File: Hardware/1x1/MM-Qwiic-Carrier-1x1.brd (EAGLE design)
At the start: 80 x 35.6 mm, 87 parts, among them J15 MICROMOD-2222-C, J2 QWIIC_RIGHT_ANGLE, J5 Vertical Qwiic Connector, U1 MCP73831, U5 AP7361C-33FGEUDFN-8

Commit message: Run of engineering checklist
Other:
- board text added: "v10"
- board text removed: "v01"
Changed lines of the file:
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@@
 <board>
 <plain>
-<wire x1="0" y1="0" x2="0" y2="35.56" width="0.254" layer="20"/>
-<wire x1="0" y1="35.56" x2="80.01" y2="35.56" width="0.254" layer="20"/>
-<wire x1="80.01" y1="35.56" x2="80.01" y2="0" width="0.254" layer="20"/>
-<wire x1="80.01" y1="0" x2="0" y2="0" width="0.254" layer="20"/>
-<text x="7.62" y="1.016" size="1.27" layer="16" font="vector" ratio="20" rot="MR180" align="center">v01</text>
+<wire x1="0" y1="0" x2="0" y2="35.56" width="0.2032" layer="20"/>
+<wire x1="0" y1="35.56" x2="80.01" y2="35.56" width="0.2032" layer="20"/>
+<wire x1="80.01" y1="35.56" x2="80.01" y2="0" width="0.2032" layer="20"/>
+<wire x1="80.01" y1="0" x2="0" y2="0" width="0.2032" layer="20"/>
+<text x="7.62" y="1.016" size="1.27" layer="16" font="vector" ratio="20" rot="MR180" align="center">v10</text>
 <wire x1="27.94" y1="28.829" x2="44.185" y2="28.829" width="0.2032" layer="21"/>
 <wire x1="44.185" y1="28.829" x2="44.185" y2="6.731" width="0.2032" layer="21"/>

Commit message: Changes from design review
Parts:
- J6: device SparkFun-Connectors:1X08_NO_SILK -> SparkFun-Connectors:1X09_NO_SILK
- moved J6 2.54 mm to (22.9, 34.3)
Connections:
- net 3.3V: now also J6.1
- net D0: now also J6.4; no longer J6.3
- net D1: now also J6.5; no longer J6.4
- net GND: now also J6.2; no longer J6.1
- net I2C_!INT!: now also J6.3; no longer J6.2
- net SPI_!CS!: now also J6.9; no longer J6.8
- net SPI_CIPO: now also J6.6; no longer J6.5
- net SPI_COPI: now also J6.7; no longer J6.6
- net SPI_SCK: now also J6.8; no longer J6.7
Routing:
- net 3.3V: track 78.8 -> 82.8 mm
- net VIN: track 30.6 -> 29.3 mm
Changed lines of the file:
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@@
 <layer number="29" name="tStop" color="7" fill="3" visible="no" active="yes"/>
 <layer number="30" name="bStop" color="7" fill="6" visible="no" active="yes"/>
-<layer number="31" name="tCream" color="7" fill="4" visible="yes" active="yes"/>
+<layer number="31" name="tCream" color="7" fill="4" visible="no" active="yes"/>
 <layer number="32" name="bCream" color="7" fill="5" visible="no" active="yes"/>
 <layer number="33" name="tFinish" color="6" fill="3" visible="no" active="yes"/>
@@
 <attribute name="VALUE" x="46.212" y="5.86833125" size="0.6096" layer="27" rot="R180"/>
 </element>
-<element name="J6" library="SparkFun-Connectors" package="1X08_NO_SILK" value="" x="25.4" y="34.29" smashed="yes">
-<attribute name="NAME" x="24.13" y="35.687" size="0.6096" layer="25" font="vector" ratio="20"/>
-<attribute name="PROD_ID" value="CONN-08438" x="25.4" y="34.29" size="1.778" layer="27" font="vector" ratio="15" display="off"/>
-<attribute name="VALUE" x="24.13" y="32.258" size="0.6096" layer="27" font="vector" ratio="20"/>
-</element>
 <element name="U$5" library="SparkFun-Boards" package="QWIIC_BOARD_MOUNT_SMD_STANDOFFS" value="QWIIC_BOARD_OUTLINESTANDOFF" x="62.23" y="17.78" smashed="yes"/>
 <element name="U$10" library="output" package="QWIIC_CARRIER_#_1X10" value="" x="51.308" y="2.413" smashed="yes"/>
@@
 <element name="U$20" library="output" package="#D1#0" value="" x="33.02" y="30.734" smashed="yes" rot="R90"/>
 <element name="U$21" library="output" package="#D1#0" value="" x="33.02" y="30.734" smashed="yes" rot="MR90"/>
+<element name="J6" library="SparkFun-Connectors" package="1X09_NO_SILK" value="" x="22.86" y="34.29" smashed="yes">
+<attribute name="NAME" x="21.59" y="35.687" size="0.6096" layer="25" font="vector" ratio="20"/>
+<attribute name="VALUE" x="21.59" y="32.258" size="0.6096" layer="27" font="vector" ratio="20"/>
+</element>
 </elements>
 <signals>
@@
 <contactref element="J4" pad="2"/>
 <contactref element="J5" pad="1"/>
-<contactref element="J6" pad="1"/>
 <via x="17.526" y="27.94" extent="1-16" drill="0.3048"/>
 <via x="3.81" y="24.13" extent="1-16" drill="0.3048"/>
@@
 <via x="20.447" y="16.637" extent="1-16" drill="0.3048"/>
 <via x="24.638" y="17.272" extent="1-16" drill="0.3048"/>
+<contactref element="J6" pad="2"/>
 </signal>
 <signal name="3.3V">
@@
 <wire x1="24.6507" y1="26.0477" x2="23.5077" y2="26.0477" width="0.4064" layer="1"/>
 <wire x1="23.5077" y1="26.0477" x2="23.5077" y2="10.738625" width="0.4064" layer="1"/>
-<wire x1="15.875" y1="31.242" x2="20.32" y2="31.242" width="0.4064" layer="16"/>
 <via x="23.5077" y="26.0477" extent="1-16" drill="0.3048"/>
-<wire x1="23.5077" y1="26.0477" x2="22.6681125" y2="26.0477" width="0.4064" layer="16"/>
-<wire x1="22.6681125" y1="26.0477" x2="22.314" y2="26.4018125" width="0.4064" layer="16"/>
-<wire x1="20.32" y1="31.242" x2="22.314" y2="29.248" width="0.4064" layer="16"/>
-<wire x1="22.314" y1="29.248" x2="22.314" y2="26.4018125" width="0.4064" layer="16"/>
 <wire x1="37.6" y1="5.08" x2="37.6" y2="3.437" width="0.4064" layer="1"/>
 <wire x1="37.6" y1="3.437" x2="37.592" y2="3.429" width="0.4064" layer="1"/>
@@
 <wire x1="26.405" y1="8.78" x2="27.542" y2="8.78" width="0.2032" layer="1"/>
 <wire x1="27.542" y1="8.78" x2="35.162" y2="8.78" width="0.4064" layer="1"/>
+<contactref element="J6" pad="1"/>
+<wire x1="22.86" y1="34.29" x2="22.86" y2="31.242" width="0.4064" layer="16"/>
+<wire x1="22.86" y1="31.242" x2="22.86" y2="26.6954" width="0.4064" layer="16"/>
+<wire x1="22.86" y1="26.6954" x2="23.5077" y2="26.0477" width="0.4064" layer="16"/>
+<wire x1="15.875" y1="31.242" x2="22.86" y2="31.242" width="0.4064" layer="16"/>
 </signal>
 <signal name="USB_D-">
@@
 <wire x1="13.97" y1="11.85" x2="13.97" y2="10.668" width="0.4064" layer="1"/>
 <via x="13.97" y="10.668" extent="1-16" drill="0.3048"/>
-<wire x1="13.97" y1="10.668" x2="12.192" y2="10.668" width="0.4064" layer="16"/>
-<wire x1="10.668" y1="12.192" x2="9.906" y2="12.192" width="0.4064" layer="16"/>
-<wire x1="9.906" y1="12.192" x2="9.525" y2="12.573" width="0.4064" layer="16"/>
-<wire x1="9.525" y1="12.573" x2="9.525" y2="14.224" width="0.4064" layer="16"/>
-<wire x1="9.7885" y1="14.4875" x2="10.2965" y2="14.4875" width="0.4064" layer="16"/>
-<wire x1="9.7885" y1="14.4875" x2="9.525" y2="14.224" width="0.4064" layer="16"/>
 <via x="10.2965" y="14.4875" extent="1-16" drill="0.3048"/>
-<wire x1="12.192" y1="10.668" x2="10.668" y2="12.192" width="0.4064" layer="16"/>
 <wire x1="13.97" y1="10.668" x2="13.97" y2="10.65786875" width="0.2032" layer="1"/>
 <wire x1="14.09786875" y1="10.53" x2="13.97" y2="10.65786875" width="0.2032" layer="1"/>
@@
 <wire x1="10.03" y1="21.968" x2="10.03" y2="19.05" width="0.4064" layer="1"/>
 <wire x1="11.43" y1="23.368" x2="10.03" y2="21.968" width="0.4064" layer="1"/>
+<wire x1="10.2965" y1="14.4875" x2="12.1825" y2="14.4875" width="0.4064" layer="16"/>
+<wire x1="12.1825" y1="14.4875" x2="13.97" y2="12.7" width="0.4064" layer="16"/>
+<wire x1="13.97" y1="12.7" x2="13.97" y2="10.668" width="0.4064" layer="16"/>
 </signal>
 <signal name="N$1">
@@
 </signal>
 <signal name="I2C_!INT!">
-<contactref element="J6" pad="2"/>
 <contactref element="J15" pad="16"/>
-<wire x1="27.94" y1="34.29" x2="29.591" y2="32.639" width="0.2032" layer="1"/>
-<wire x1="29.591" y1="32.639" x2="29.591" y2="17.018" width="0.2032" layer="1"/>
+<wire x1="29.591" y1="31.75" x2="29.591" y2="17.018" width="0.2032" layer="1"/>
 <wire x1="27.94" y1="15.367" x2="25.273" y2="15.367" width="0.2032" layer="1"/>
 <wire x1="25.273" y1="15.367" x2="24.511" y2="14.605" width="0.2032" layer="1"/>
@@
 <wire x1="24.511" y1="14.605" x2="24.511" y2="12.954" width="0.2032" layer="1"/>
 <wire x1="24.511" y1="12.954" x2="25.185" y2="12.28" width="0.2032" layer="1"/>
+<contactref element="J6" pad="3"/>
+<wire x1="27.94" y1="34.29" x2="29.591" y2="32.639" width="0.2032" layer="1"/>
+<wire x1="29.591" y1="32.639" x2="29.591" y2="31.75" width="0.2032" layer="1"/>
 </signal>
 <signal name="D0">
-<contactref element="J6" pad="3"/>
 <contactref element="J15" pad="10"/>
-<wire x1="30.48" y1="34.29" x2="30.48" y2="13.716" width="0.2032" layer="1"/>
 <via x="30.48" y="13.716" extent="1-16" drill="0.3048"/>
 <wire x1="30.48" y1="13.716" x2="30.48" y2="11.684" width="0.2032" layer="16"/>
@@
 <wire x1="27.97213125" y1="10.668" x2="27.86013125" y2="10.78" width="0.2032" layer="1"/>
 <wire x1="27.86013125" y1="10.78" x2="26.405" y2="10.78" width="0.2032" layer="1"/>
+<contactref element="J6" pad="4"/>
+<wire x1="30.48" y1="34.29" x2="30.48" y2="13.716" width="0.2032" layer="1"/>
 </signal>
 <signal name="D1">
-<contactref element="J6" pad="4"/>
 <contactref element="J15" pad="18"/>
+<wire x1="31.322" y1="12.78" x2="26.405" y2="12.78" width="0.2032" layer="1"/>
+<contactref element="J6" pad="5"/>
+<wire x1="32.766" y1="14.224" x2="31.322" y2="12.78" width="0.2032" layer="1"/>
 <wire x1="33.02" y1="34.29" x2="33.02" y2="14.478" width="0.2032" layer="1"/>
-<wire x1="31.322" y1="12.78" x2="26.405" y2="12.78" width="0.2032" layer="1"/>
-<wire x1="33.02" y1="14.478" x2="31.322" y2="12.78" width="0.2032" layer="1"/>
+<wire x1="33.02" y1="14.478" x2="32.766" y2="14.224" width="0.2032" layer="1"/>
 </signal>
 <signal name="SPI_SCK">
-<contactref element="J6" pad="7"/>
 <contactref element="J15" pad="57"/>
 <wire x1="38.735" y1="22.606" x2="20.828" y2="22.606" width="0.2032" layer="16"/>
@@
 <wire x1="19.89083125" y1="22.6187" x2="19.80213125" y2="22.53" width="0.2032" layer="1"/>
 <wire x1="18.855" y1="22.53" x2="19.80213125" y2="22.53" width="0.2032" layer="1"/>
+<wire x1="40.64" y1="24.511" x2="38.735" y2="22.606" width="0.2032" layer="16"/>
+<contactref element="J6" pad="8"/>
 <wire x1="40.64" y1="34.29" x2="40.64" y2="24.511" width="0.2032" layer="16"/>
-<wire x1="40.64" y1="24.511" x2="38.735" y2="22.606" width="0.2032" layer="16"/>
 </signal>
 <signal name="SPI_!CS!">
-<contactref element="J6" pad="8"/>
 <contactref element="J15" pad="55"/>
-<wire x1="43.18" y1="34.29" x2="43.18" y2="25.019" width="0.2032" layer="16"/>
 <wire x1="40.132" y1="21.971" x2="20.193" y2="21.971" width="0.2032" layer="16"/>
 <via x="20.193" y="21.971" extent="1-16" drill="0.3048"/>
@@
 <wire x1="18.914" y1="21.971" x2="18.855" y2="22.03" width="0.2032" layer="1"/>
 <wire x1="43.18" y1="25.019" x2="40.132" y2="21.971" width="0.2032" layer="16"/>
+<contactref element="J6" pad="9"/>
+<wire x1="43.18" y1="34.29" x2="43.18" y2="25.019" width="0.2032" layer="16"/>
 </signal>
 <signal name="SPI_COPI">
 <contactref element="J15" pad="59"/>
-<contactref element="J6" pad="6"/>
-<wire x1="38.1" y1="34.29" x2="38.1" y2="25.019" width="0.2032" layer="16"/>
 <wire x1="38.1" y1="25.019" x2="36.3093" y2="23.2283" width="0.2032" layer="16"/>
 <wire x1="36.3093" y1="23.2283" x2="20.2522" y2="23.2283" width="0.2032" layer="16"/>
@@
 <wire x1="20.2522" y1="23.2283" x2="20.0539" y2="23.03" width="0.2032" layer="1"/>
 <wire x1="20.0539" y1="23.03" x2="18.855" y2="23.03" width="0.2032" layer="1"/>
+<contactref element="J6" pad="7"/>
+<wire x1="38.1" y1="34.29" x2="38.1" y2="25.019" width="0.2032" layer="16"/>
 </signal>
 <signal name="SPI_CIPO">
 <contactref element="J15" pad="61"/>
-<contactref element="J6" pad="5"/>
-<wire x1="35.56" y1="34.29" x2="35.56" y2="25.273" width="0.2032" layer="16"/>
 <wire x1="34.1249" y1="23.8379" x2="21.082" y2="23.8379" width="0.2032" layer="16"/>
 <via x="21.082" y="23.8379" extent="1-16" drill="0.3048"/>
@@
 <wire x1="21.082" y1="23.8379" x2="19.99969375" y2="23.8379" width="0.2032" layer="1"/>
 <wire x1="35.56" y1="25.273" x2="34.1249" y2="23.8379" width="0.2032" layer="16"/>
+<contactref element="J6" pad="6"/>
+<wire x1="35.56" y1="34.29" x2="35.56" y2="25.273" width="0.2032" layer="16"/>
 </signal>
 <signal name="V_USB_2">

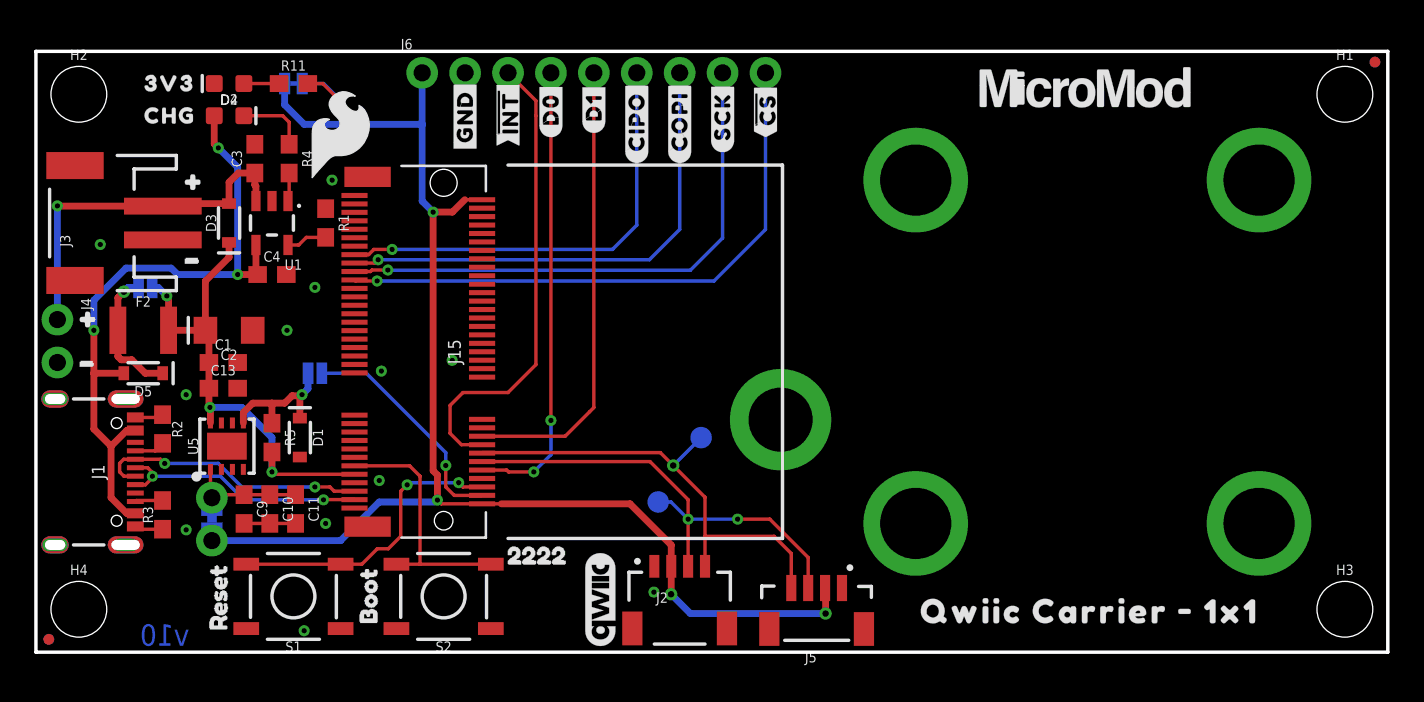
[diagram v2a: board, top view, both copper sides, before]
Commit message: Silk changes from red board design review
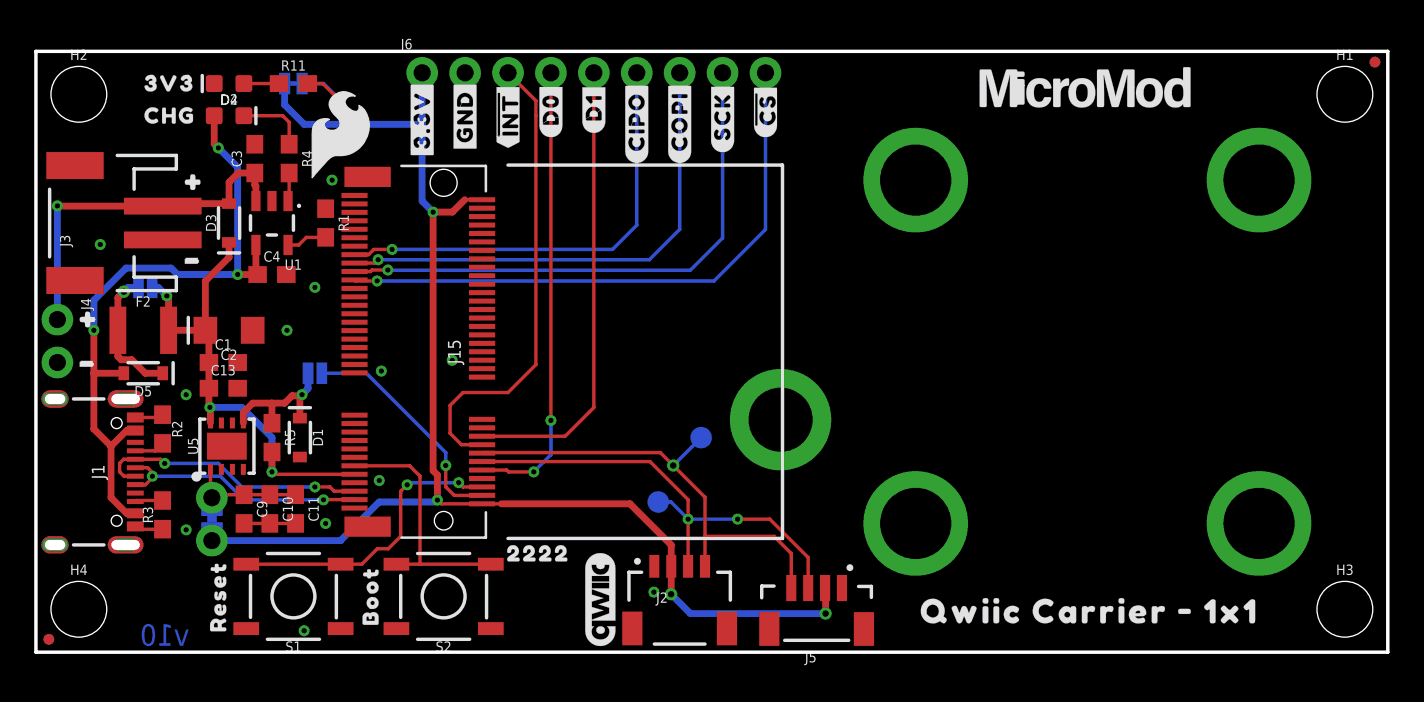
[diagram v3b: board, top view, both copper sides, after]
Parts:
- removed U$19: (no value), buzzard_labels (10):BOOT2
- removed U$2: (no value), buzzard_labels (9):RESET3
- removed U$55: (no value), buzzard_labels (9):22229
- added U$30: (no value), output:RESET0
- added U$31: (no value), output:BOOT0
- added U$34: (no value), output:22220
- added U$35, U$38: (no value), output:#3#3V#0
- moved U$15 0.13 mm to (27.9, 29.8)
- moved U$16 0.13 mm to (27.9, 29.8)
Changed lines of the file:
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@@
 <?xml version="1.0" encoding="utf-8"?>
 <!DOCTYPE eagle SYSTEM "eagle.dtd">
-<eagle version="9.5.2">
+<eagle version="9.6.2">
 <drawing>
 <settings>
-<setting alwaysvectorfont="no"/>
+<setting alwaysvectorfont="yes"/>
 <setting verticaltext="up"/>
 </settings>
@@
 <attribute name="VALUE" x="24.13" y="5.969" size="0.6096" layer="27" font="vector" ratio="20" rot="R180" align="top-center"/>
 </element>
-<element name="U$2" library="buzzard_labels (9)" package="RESET3" value="" x="10.795" y="0.381" smashed="yes" rot="R90"/>
-<element name="U$19" library="buzzard_labels (10)" package="BOOT2" value="" x="19.685" y="0.762" smashed="yes" rot="R90"/>
 <element name="LOGO2" library="SparkFun-Aesthetics" package="QWIIC_5.5MM" value="QWIIC_LOGO_CONNECTOR" x="33.401" y="3.1115" smashed="yes" rot="R90"/>
 <element name="LOGO3" library="SparkFun-Aesthetics" package="OSHW-LOGO-M" value="OSHW-LOGOM" x="31.623" y="10.922" smashed="yes" rot="MR0"/>
-<element name="U$55" library="buzzard_labels (9)" package="22229" value="" x="26.962" y="5.72" smashed="yes"/>
 <element name="H5" library="SparkFun-Hardware" package="STAND-OFF-REFLOW-M2.5" value="STAND-OFF-REFLOW2.5MM_TALL" x="44.073" y="13.76" smashed="yes">
 <attribute name="PROD_ID" value="HW-14899" x="44.073" y="13.76" size="1.778" layer="27" font="vector" ratio="15" display="off"/>
@@
 <element name="U$8" library="output" package="#GND#0" value="" x="25.4" y="29.464" smashed="yes" rot="R90"/>
 <element name="U$14" library="output" package="#GND#0" value="" x="25.4" y="29.464" smashed="yes" rot="MR90"/>
-<element name="U$15" library="output" package="##INT##0" value="" x="27.94" y="29.972" smashed="yes" rot="R90"/>
-<element name="U$16" library="output" package="##INT##0" value="" x="27.94" y="29.972" smashed="yes" rot="MR90"/>
 <element name="U$22" library="output" package="#CIPO#0" value="" x="35.56" y="28.956" smashed="yes" rot="R90"/>
 <element name="U$23" library="output" package="#CIPO#0" value="" x="35.56" y="28.956" smashed="yes" rot="MR90"/>
@@
 <element name="U$36" library="buzzard_labels (1)" package="#0" value="" x="1.143" y="17.399" smashed="yes"/>
 <element name="U$37" library="buzzard_labels (1)" package="#0" value="" x="7.366" y="23.495" smashed="yes"/>
-<element name="U$28" library="output" package="##CS##0" value="" x="43.18" y="30.48" smashed="yes" rot="R90"/>
-<element name="U$29" library="output" package="##CS##0" value="" x="43.18" y="30.48" smashed="yes" rot="MR90"/>
 <element name="U$17" library="output" package="#D0#0" value="" x="30.48" y="30.48" smashed="yes" rot="R90"/>
 <element name="U$18" library="output" package="#D0#0" value="" x="30.48" y="30.48" smashed="yes" rot="MR90"/>
@@
 <attribute name="VALUE" x="21.59" y="32.258" size="0.6096" layer="27" font="vector" ratio="20"/>
 </element>
+<element name="U$30" library="output" package="RESET0" value="" x="10.795" y="0.508" smashed="yes" rot="R90"/>
+<element name="U$31" library="output" package="BOOT0" value="" x="19.812" y="0.889" smashed="yes" rot="R90"/>
+<element name="U$34" library="output" package="22220" value="" x="27.178" y="5.842" smashed="yes"/>
+<element name="U$35" library="output" package="#3#3V#0" value="" x="22.86" y="29.083" smashed="yes" rot="R90"/>
+<element name="U$38" library="output" package="#3#3V#0" value="" x="22.86" y="29.083" smashed="yes" rot="MR90"/>
+<element name="U$28" library="output" package="##CS##0" value="" x="43.18" y="30.48" smashed="yes" rot="R90"/>
+<element name="U$29" library="output" package="##CS##0" value="" x="43.18" y="30.48" smashed="yes" rot="MR90"/>
+<element name="U$15" library="output" package="##INT##0" value="" x="27.94" y="29.845" smashed="yes" rot="R90"/>
+<element name="U$16" library="output" package="##INT##0" value="" x="27.94" y="29.845" smashed="yes" rot="MR90"/>
 </elements>
 <signals>
